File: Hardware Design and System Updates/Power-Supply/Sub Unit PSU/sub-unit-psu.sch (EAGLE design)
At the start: 5 parts, among them U1 BA033CC0FP-E2TO252-3_ROM

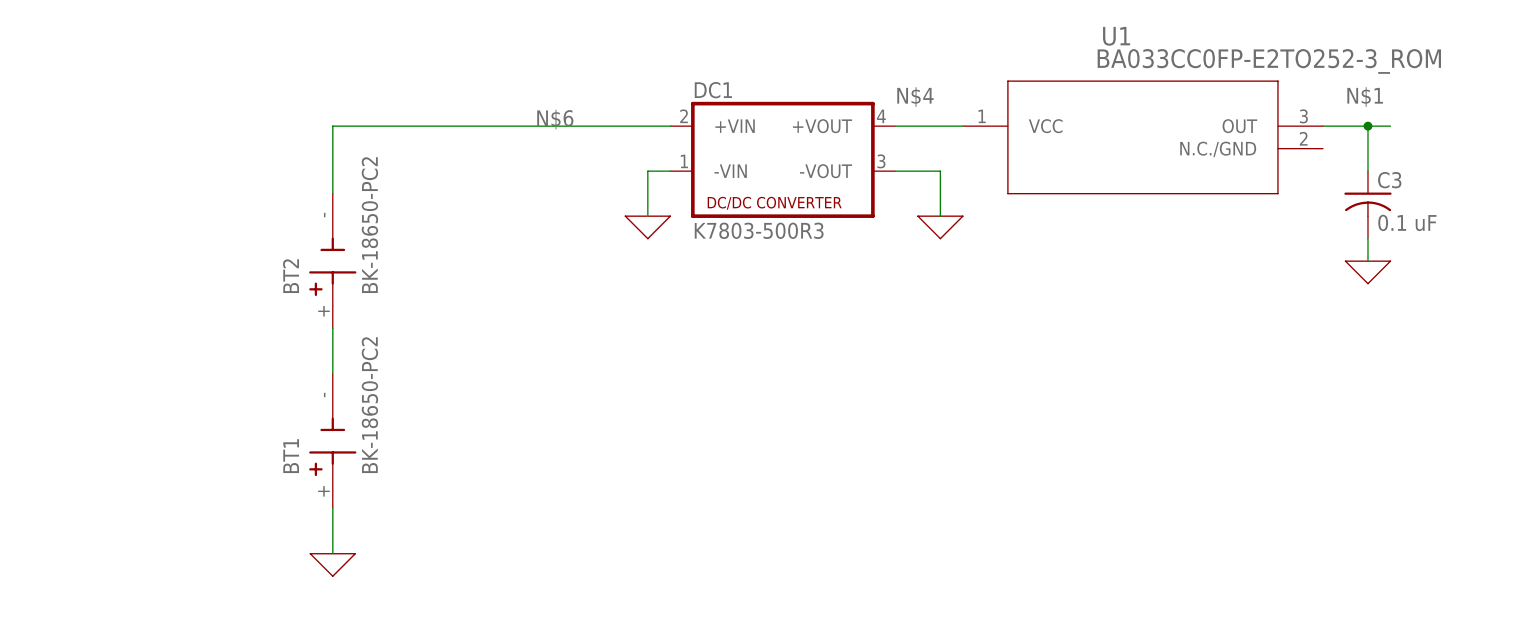
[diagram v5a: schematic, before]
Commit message: Added 5V regulator to PSU schematics
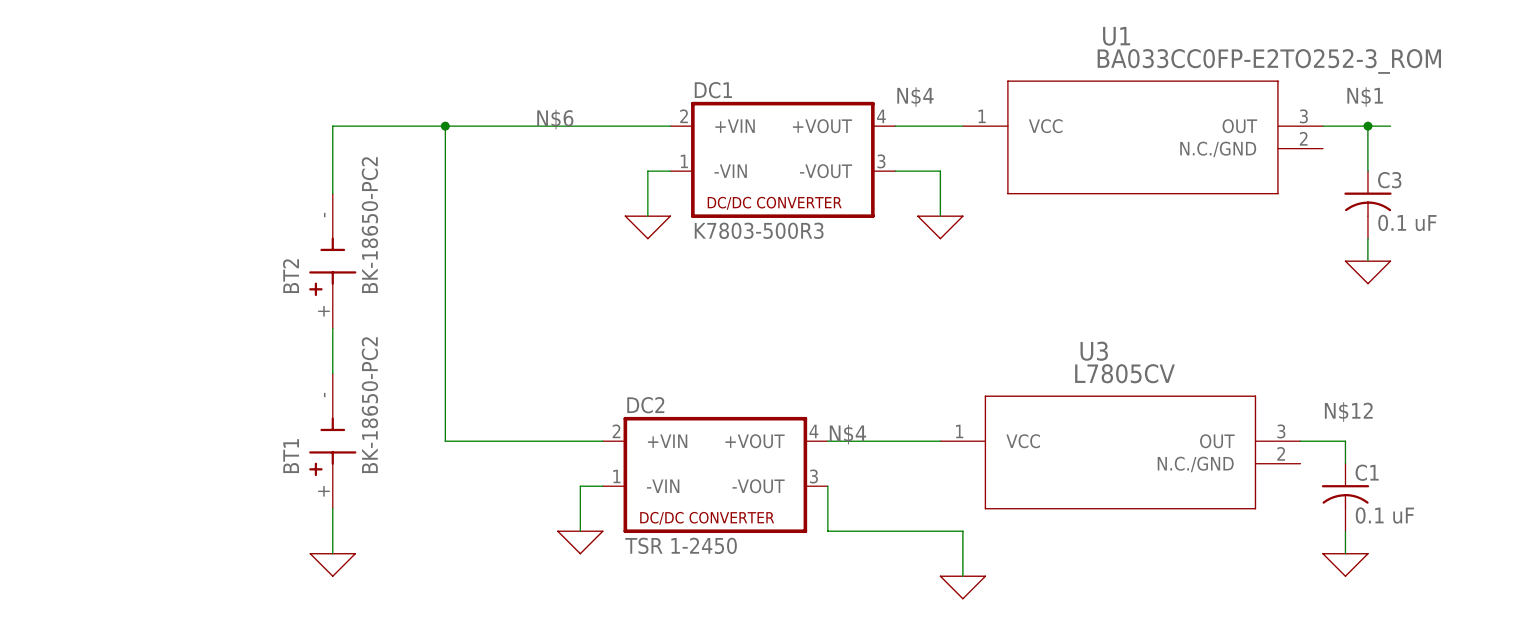
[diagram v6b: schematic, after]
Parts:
- added C1: 0.1 uF, rcl:C-US050-024X044
- added DC2: TSR 1-2450, dc-dc-converter:NME
- added U3: L7805CV, 2023-03-08_12-17-23_Library:BA033CC0FP-E2TO252-3_ROM
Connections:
- new net N$12: C1.1, U3.OUT
- net 0: now also C1.2, DC2.-VIN, DC2.-VOUT
- net N$4: now also DC2.+VOUT, U3.VCC
- net N$6: now also DC2.+VIN
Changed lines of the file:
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@@
 <layer number="106" name="bPlate" color="4" fill="1" visible="yes" active="yes"/>
 <layer number="107" name="Crop" color="5" fill="1" visible="yes" active="yes"/>
+<layer number="108" name="fp8" color="7" fill="1" visible="no" active="yes"/>
+<layer number="109" name="fp9" color="7" fill="1" visible="no" active="yes"/>
+<layer number="110" name="fp0" color="7" fill="1" visible="no" active="yes"/>
 <layer number="111" name="tGTest" color="7" fill="1" visible="yes" active="yes"/>
 <layer number="112" name="bGTest" color="7" fill="1" visible="yes" active="yes"/>
+<layer number="113" name="ReferenceLS" color="7" fill="1" visible="no" active="no"/>
 <layer number="116" name="Patch_BOT" color="9" fill="4" visible="yes" active="yes"/>
 <layer number="117" name="mPads" color="7" fill="1" visible="yes" active="yes"/>
@@
 <layer number="149" name="mReference" color="7" fill="1" visible="yes" active="yes"/>
 <layer number="150" name="References" color="7" fill="1" visible="yes" active="yes"/>
+<layer number="151" name="HeatSink" color="7" fill="1" visible="no" active="yes"/>
 <layer number="152" name="mbDocu" color="7" fill="1" visible="yes" active="yes"/>
+<layer number="153" name="FabDoc1" color="6" fill="1" visible="no" active="no"/>
+<layer number="154" name="FabDoc2" color="2" fill="1" visible="no" active="no"/>
+<layer number="155" name="FabDoc3" color="7" fill="15" visible="no" active="no"/>
 <layer number="191" name="mNets" color="7" fill="1" visible="yes" active="yes"/>
 <layer number="192" name="mBusses" color="7" fill="1" visible="yes" active="yes"/>
@@
 <layer number="207" name="207bmp" color="8" fill="1" visible="yes" active="yes"/>
 <layer number="208" name="208bmp" color="9" fill="1" visible="yes" active="yes"/>
+<layer number="209" name="209bmp" color="7" fill="1" visible="no" active="yes"/>
+<layer number="210" name="210bmp" color="7" fill="1" visible="no" active="yes"/>
+<layer number="211" name="211bmp" color="7" fill="1" visible="no" active="yes"/>
+<layer number="212" name="212bmp" color="7" fill="1" visible="no" active="yes"/>
+<layer number="213" name="213bmp" color="7" fill="1" visible="no" active="yes"/>
+<layer number="214" name="214bmp" color="7" fill="1" visible="no" active="yes"/>
+<layer number="215" name="215bmp" color="7" fill="1" visible="no" active="yes"/>
 <layer number="216" name="SMD16" color="3" fill="11" visible="yes" active="yes"/>
+<layer number="217" name="217bmp" color="18" fill="1" visible="no" active="no"/>
+<layer number="218" name="218bmp" color="19" fill="1" visible="no" active="no"/>
+<layer number="219" name="219bmp" color="20" fill="1" visible="no" active="no"/>
+<layer number="220" name="220bmp" color="21" fill="1" visible="no" active="no"/>
+<layer number="221" name="221bmp" color="22" fill="1" visible="no" active="no"/>
+<layer number="222" name="222bmp" color="23" fill="1" visible="no" active="no"/>
+<layer number="223" name="223bmp" color="24" fill="1" visible="no" active="no"/>
+<layer number="224" name="224bmp" color="25" fill="1" visible="no" active="no"/>
+<layer number="225" name="225bmp" color="7" fill="1" visible="yes" active="yes"/>
+<layer number="226" name="226bmp" color="7" fill="1" visible="yes" active="yes"/>
+<layer number="227" name="227bmp" color="7" fill="1" visible="yes" active="yes"/>
+<layer number="228" name="228bmp" color="7" fill="1" visible="yes" active="yes"/>
+<layer number="229" name="229bmp" color="7" fill="1" visible="yes" active="yes"/>
+<layer number="230" name="230bmp" color="7" fill="1" visible="yes" active="yes"/>
 <layer number="231" name="Eagle3D_PG1" color="7" fill="1" visible="yes" active="yes"/>
 <layer number="232" name="Eagle3D_PG2" color="7" fill="1" visible="yes" active="yes"/>
 <layer number="233" name="Eagle3D_PG3" color="7" fill="1" visible="yes" active="yes"/>
+<layer number="248" name="Housing" color="7" fill="1" visible="no" active="yes"/>
+<layer number="249" name="Edge" color="7" fill="1" visible="no" active="yes"/>
 <layer number="250" name="Descript" color="3" fill="1" visible="yes" active="yes"/>
 <layer number="251" name="SMDround" color="12" fill="11" visible="yes" active="yes"/>
@@
 <part name="C3" library="rcl" library_urn="urn:adsk.eagle:library:334" deviceset="C-US" device="050-024X044" package3d_urn="urn:adsk.eagle:package:23643/1" value="0.1 uF"/>
 <part name="X_10" library="ngspice-simulation" library_urn="urn:adsk.eagle:library:527439" deviceset="GND" device=""/>
+<part name="DC2" library="dc-dc-converter" library_urn="urn:adsk.eagle:library:208" deviceset="NME" device="" package3d_urn="urn:adsk.eagle:package:12313/1" value="TSR 1-2450"/>
+<part name="X_6" library="ngspice-simulation" library_urn="urn:adsk.eagle:library:527439" deviceset="GND" device=""/>
+<part name="U3" library="2023-03-08_12-17-23_Library" deviceset="BA033CC0FP-E2" device="TO252-3_ROM" value="L7805CV"/>
+<part name="X_8" library="ngspice-simulation" library_urn="urn:adsk.eagle:library:527439" deviceset="GND" device=""/>
+<part name="C1" library="rcl" library_urn="urn:adsk.eagle:library:334" deviceset="C-US" device="050-024X044" package3d_urn="urn:adsk.eagle:package:23643/1" value="0.1 uF"/>
+<part name="X_3" library="ngspice-simulation" library_urn="urn:adsk.eagle:library:527439" deviceset="GND" device=""/>
 </parts>
 <sheets>
@@
 </instance>
 <instance part="X_10" gate="G$1" x="233.68" y="134.62" smashed="yes"/>
+<instance part="DC2" gate="G$1" x="160.02" y="111.76" smashed="yes">
+<attribute name="NAME" x="149.86" y="117.475" size="1.778" layer="95"/>
+<attribute name="VALUE" x="149.86" y="101.6" size="1.778" layer="96"/>
+</instance>
+<instance part="X_6" gate="G$1" x="144.78" y="104.14" smashed="yes"/>
+<instance part="U3" gate="A" x="182.88" y="114.3" smashed="yes">
+<attribute name="NAME" x="201.0146" y="123.4186" size="2.083" layer="95" ratio="6"/>
+<attribute name="VALUE" x="200.3752" y="120.8786" size="2.083" layer="96" ratio="6"/>
+</instance>
+<instance part="X_8" gate="G$1" x="187.96" y="99.06" smashed="yes"/>
+<instance part="C1" gate="G$1" x="231.14" y="109.22" smashed="yes">
+<attribute name="NAME" x="232.156" y="109.855" size="1.778" layer="95"/>
+<attribute name="VALUE" x="232.156" y="105.029" size="1.778" layer="96"/>
+</instance>
+<instance part="X_3" gate="G$1" x="231.14" y="101.6" smashed="yes"/>
 </instances>
 <busses>
@@
 <wire x1="233.68" y1="134.62" x2="233.68" y2="137.16" width="0.1524" layer="91"/>
 </segment>
+<segment>
+<pinref part="X_6" gate="G$1" pin="0"/>
+<pinref part="DC2" gate="G$1" pin="-VIN"/>
+<wire x1="144.78" y1="104.14" x2="144.78" y2="109.22" width="0.1524" layer="91"/>
+<wire x1="144.78" y1="109.22" x2="147.32" y2="109.22" width="0.1524" layer="91"/>
+</segment>
+<segment>
+<pinref part="DC2" gate="G$1" pin="-VOUT"/>
+<wire x1="172.72" y1="109.22" x2="172.72" y2="104.14" width="0.1524" layer="91"/>
+<wire x1="172.72" y1="104.14" x2="187.96" y2="104.14" width="0.1524" layer="91"/>
+<pinref part="X_8" gate="G$1" pin="0"/>
+<wire x1="187.96" y1="99.06" x2="187.96" y2="104.14" width="0.1524" layer="91"/>
+</segment>
+<segment>
+<pinref part="X_3" gate="G$1" pin="0"/>
+<pinref part="C1" gate="G$1" pin="2"/>
+<wire x1="231.14" y1="101.6" x2="231.14" y2="104.14" width="0.1524" layer="91"/>
+</segment>
 </net>
 <net name="N$4" class="0">
@@
 <label x="180.34" y="152.4" size="1.778" layer="95"/>
 <pinref part="U1" gate="A" pin="VCC"/>
+</segment>
+<segment>
+<pinref part="DC2" gate="G$1" pin="+VOUT"/>
+<wire x1="172.72" y1="114.3" x2="185.42" y2="114.3" width="0.1524" layer="91"/>
+<label x="172.72" y="114.3" size="1.778" layer="95"/>
+<pinref part="U3" gate="A" pin="VCC"/>
 </segment>
 </net>
@@
 </segment>
 </net>
-<net name="N$6" class="0">
-<segment>
-<pinref part="DC1" gate="G$1" pin="+VIN"/>
-<wire x1="116.84" y1="149.86" x2="154.94" y2="149.86" width="0.1524" layer="91"/>
-<label x="139.7" y="149.86" size="1.778" layer="95"/>
-<pinref part="BT2" gate="G$1" pin="-"/>
-<wire x1="116.84" y1="142.24" x2="116.84" y2="149.86" width="0.1524" layer="91"/>
-</segment>
-</net>
 <net name="N$2" class="0">
 <segment>
@@
 </segment>
 </net>
+<net name="N$12" class="0">
+<segment>
+<wire x1="226.06" y1="114.3" x2="231.14" y2="114.3" width="0.1524" layer="91"/>
+<label x="228.6" y="116.84" size="1.778" layer="95"/>
+<pinref part="U3" gate="A" pin="OUT"/>
+<pinref part="C1" gate="G$1" pin="1"/>
+<wire x1="231.14" y1="111.76" x2="231.14" y2="114.3" width="0.1524" layer="91"/>
+</segment>
+</net>
+<net name="N$6" class="0">
+<segment>
+<pinref part="DC2" gate="G$1" pin="+VIN"/>
+<wire x1="129.54" y1="114.3" x2="147.32" y2="114.3" width="0.1524" layer="91"/>
+<pinref part="DC1" gate="G$1" pin="+VIN"/>
+<wire x1="116.84" y1="149.86" x2="129.54" y2="149.86" width="0.1524" layer="91"/>
+<label x="139.7" y="149.86" size="1.778" layer="95"/>
+<pinref part="BT2" gate="G$1" pin="-"/>
+<wire x1="129.54" y1="149.86" x2="154.94" y2="149.86" width="0.1524" layer="91"/>
+<wire x1="116.84" y1="142.24" x2="116.84" y2="149.86" width="0.1524" layer="91"/>
+<wire x1="129.54" y1="114.3" x2="129.54" y2="149.86" width="0.1524" layer="91"/>
+<junction x="129.54" y="149.86"/>
+</segment>
+</net>
